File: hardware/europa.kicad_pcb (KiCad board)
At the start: 2 copper layers, 40.3 x 128.5 mm, 18 parts, among them J1 Left, J2 Right, J3 AudioJack2, J4 AudioJack2_Ground, J5 AudioJack2_Ground, J6 AudioJack2_Ground

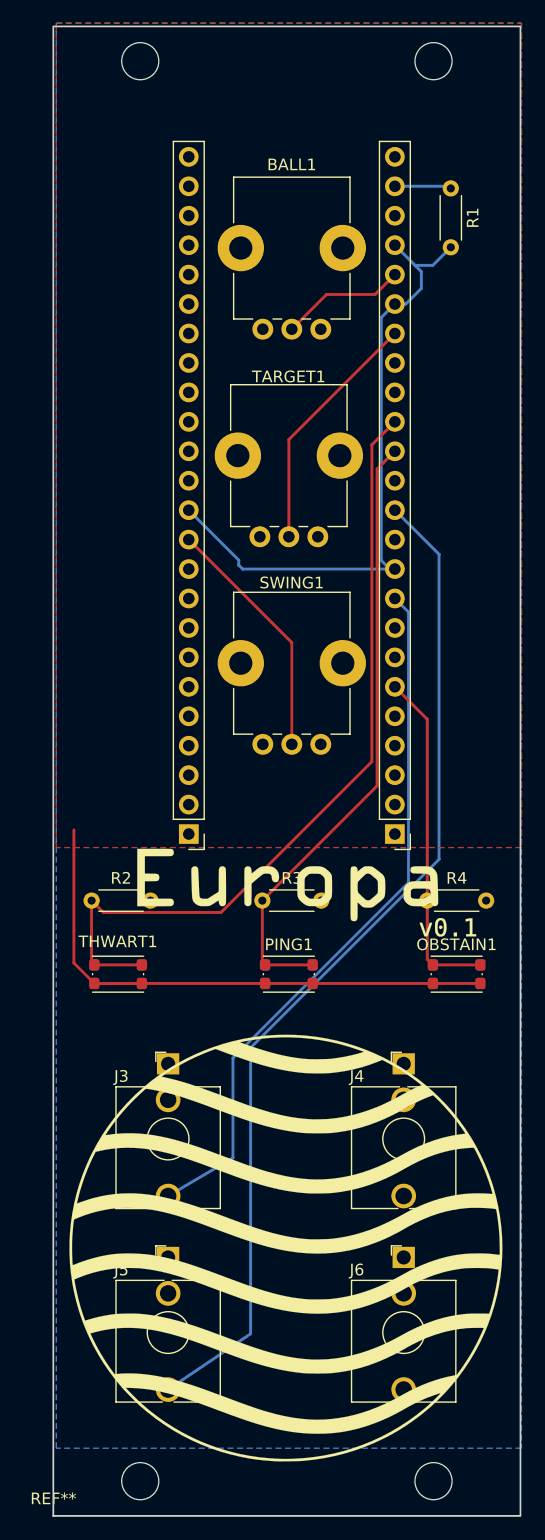
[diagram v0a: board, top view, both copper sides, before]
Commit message: Sanitized hardware layout numbering, some silkscreen mods
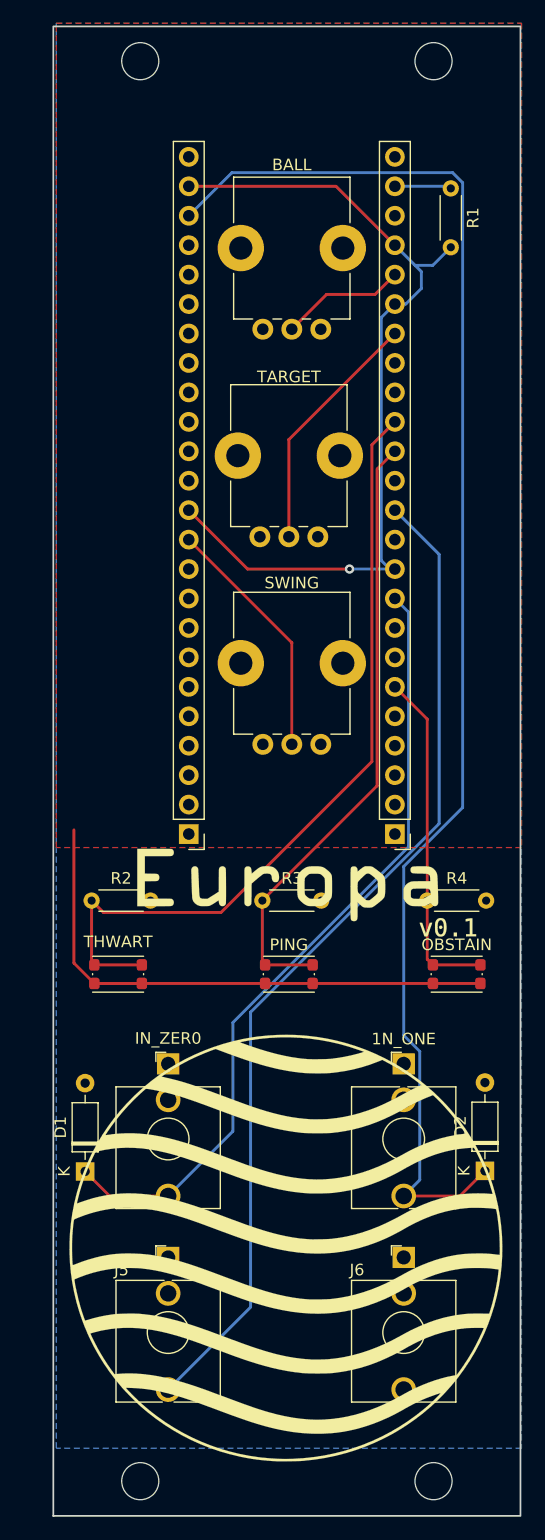
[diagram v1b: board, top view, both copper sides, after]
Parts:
- added D1: 3.3V, Diode_THT:D_DO-35_SOD27_P7.62mm_Horizontal, F.Cu at (84.3, 118.4)
- added D2: 3.3V, Diode_THT:D_DO-35_SOD27_P7.62mm_Horizontal, F.Cu at (118.8, 118.3)
- renumbered J4 to 1N_ONE, BALL1 to BALL, J3 to IN_ZER0, OBSTAIN1 to OBSTAIN, PING1 to PING, SWING1 to SWING, TARGET1 to TARGET, THWART1 to THWART
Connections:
- net AU_OUT1 renamed AU_OUT0
- 1N_ONE pad T: unconnected-(J4-PadT) -> AU_IN1
- IN_ZER0 pad T: AU_IN1 -> AU_IN0
- J1 pad 14: BUTTON2 -> BUTTON1
- J1 pad 15: BUTTON1 -> BUTTON0
- J1 pad 6: BUTTON3 -> BUTTON2
- J1 pad 9: AU_IN1 -> AU_IN0
- J2 pad 22: /IOT_51A -> AU_IN1
- J2 pad 23: /IOT_50B -> VREF
- OBSTAIN pad 1: BUTTON3 -> BUTTON2
- PING pad 1: BUTTON2 -> BUTTON1
- R2 pad 1: BUTTON1 -> BUTTON0
- R3 pad 1: BUTTON2 -> BUTTON1
- R4 pad 1: BUTTON3 -> BUTTON2
- THWART pad 1: BUTTON1 -> BUTTON0
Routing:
- net BUTTON0: track 0.00 -> 69.9 mm
- net AU_IN0: track 0.00 -> 68.7 mm
- net AU_IN1: track 61.5 -> 124.1 mm
- net BUTTON3: track 29.4 -> 0.00 mm
- net BUTTON2: track 53.2 -> 29.4 mm
- net VREF: track 55.5 -> 75.1 mm, vias 0 -> 1
- net BUTTON1: track 69.9 -> 53.2 mm
- net AU_OUT0: track 87.5 -> 86.7 mm
